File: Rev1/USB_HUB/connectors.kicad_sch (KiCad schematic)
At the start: 24 parts, among them J6 B4B-XH-A, J9 B4B-XH-A, Q1 IRLML2244TRPBF, Q2 IRLML2244TRPBF, Q3 IRLML2244TRPBF, Q4 IRLML2244TRPBF, Q5 IRLML2244TRPBF, Q7 IRLML2244TRPBF

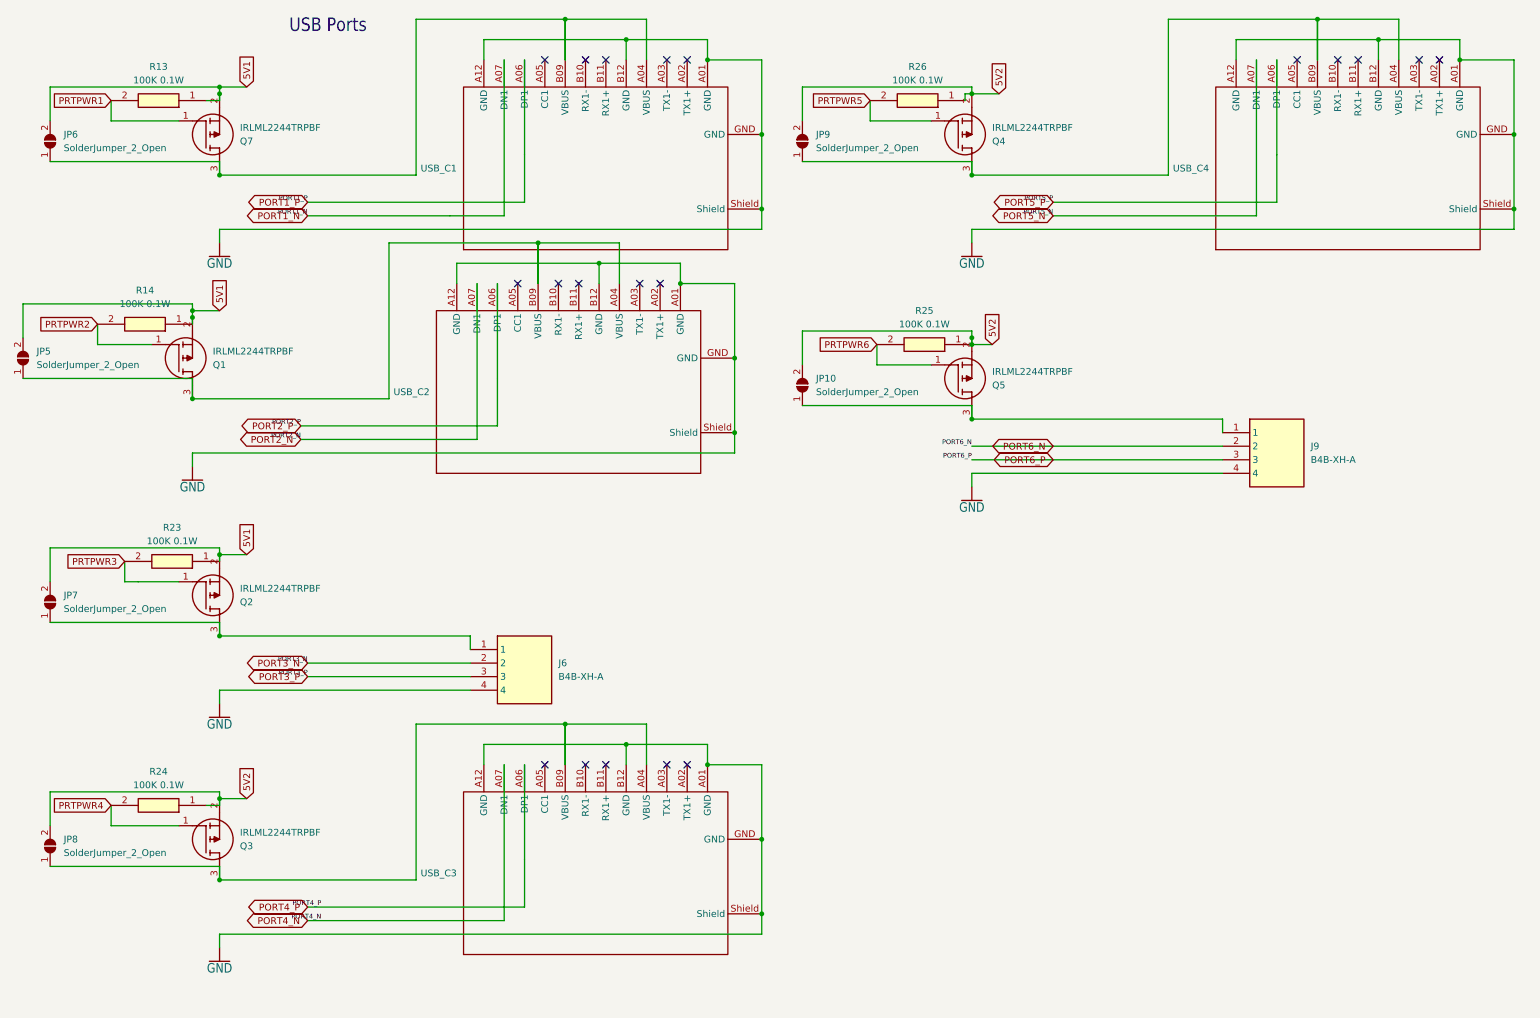
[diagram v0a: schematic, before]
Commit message: USB HUB Updated
Based on TA feedback
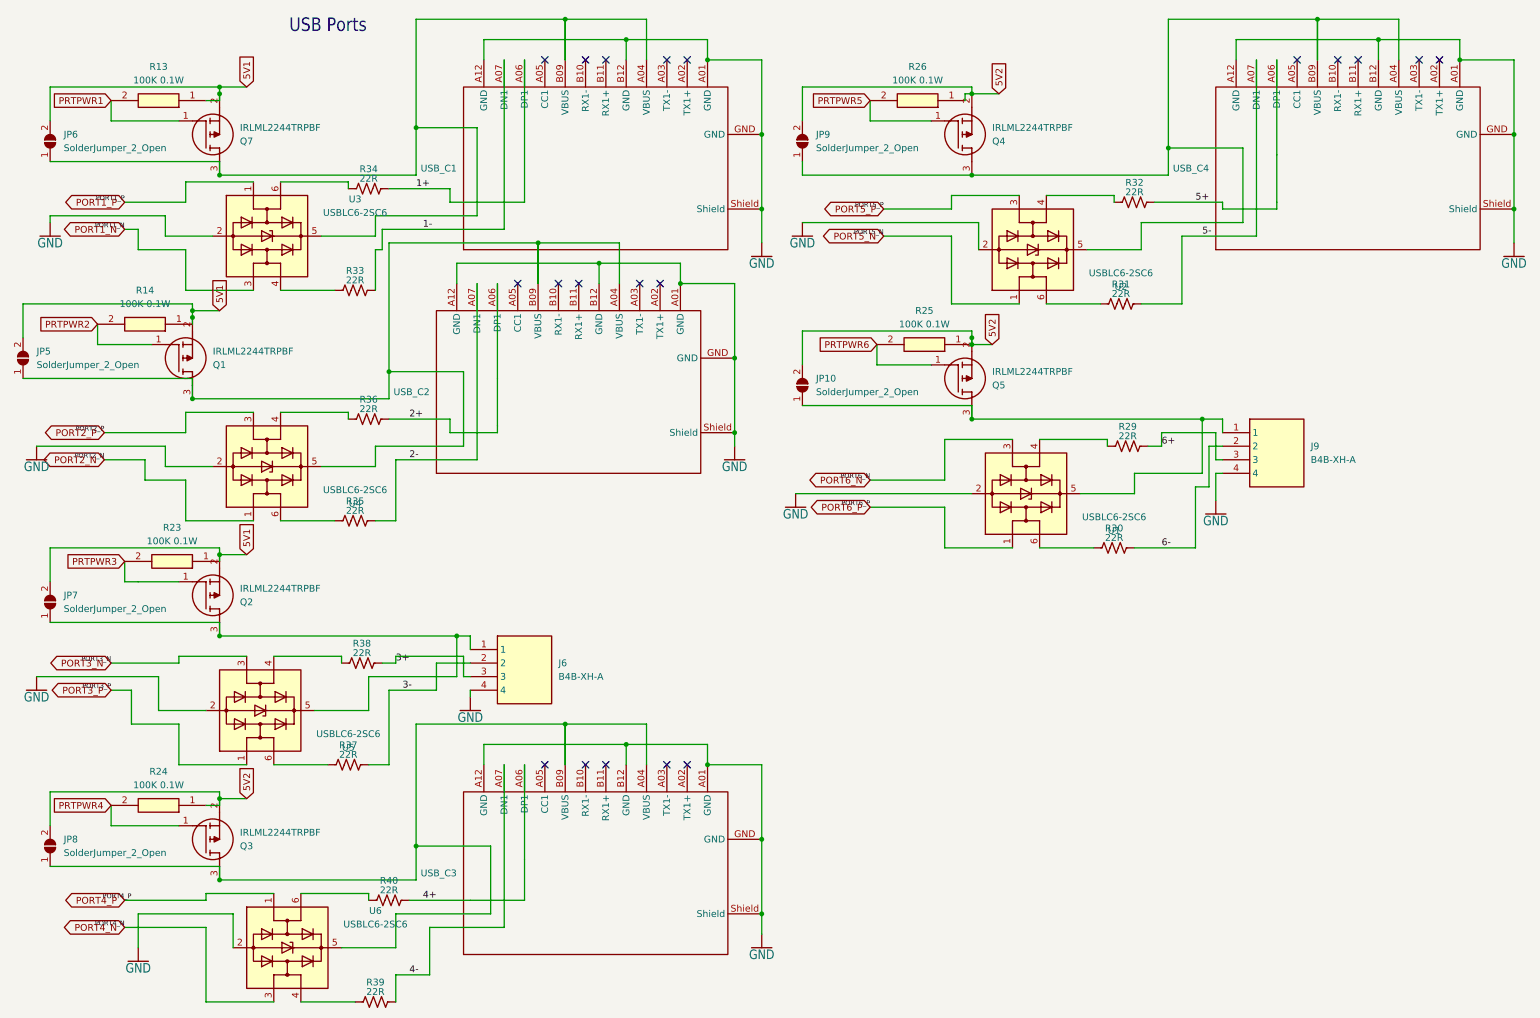
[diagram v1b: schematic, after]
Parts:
- added R29, R30, R31, R32, R33, R34, R35, R36, R37, R38, R39, R40: 22R, Resistor_SMD:R_0603_1608Metric, symbol Device:R_US
- added U1, U2, U3, U4, U5, U6: USBLC6-2SC6, Package_TO_SOT_SMD:SOT-23-6, symbol Power_Protection:USBLC6-2SC6
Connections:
- net GND: now also U1.2 (GND), U2.2 (GND), U3.2 (GND), U4.2 (GND), U5.2 (GND), U6.2 (GND)
- net PORT1_N: now also U3.3 (I/O2); no longer USB_C1.A07 (DN1)
- net PORT1_P: now also U3.1 (I/O1); no longer USB_C1.A06 (DP1)
- net PORT2_N: now also U4.1 (I/O1); no longer USB_C2.A07 (DN1)
- net PORT2_P: now also U4.3 (I/O2); no longer USB_C2.A06 (DP1)
- net PORT3_N: now also U5.3 (I/O2); no longer J6.2
- net PORT3_P: now also U5.1 (I/O1); no longer J6.3
- net PORT4_N: now also U6.3 (I/O2); no longer USB_C3.A07 (DN1)
- net PORT4_P: now also U6.1 (I/O1); no longer USB_C3.A06 (DP1)
- net PORT5_N: now also U2.1 (I/O1); no longer USB_C4.A07 (DN1)
- net PORT5_P: now also U2.3 (I/O2); no longer USB_C4.A06 (DP1)
- net PORT6_N: now also U1.3 (I/O2); no longer J9.2
- net PORT6_P: now also U1.1 (I/O1); no longer J9.3
- net at JP5.1 (A), Q1.3 (D), USB_C2.A04 (VBUS)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: now also U4.5 (VBUS)
- net at JP9.1 (A), Q4.3 (D), USB_C4.A04 (VBUS)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: now also U2.5 (VBUS)
- net at JP8.1 (A), Q3.3 (D), USB_C3.A04 (VBUS)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: now also U6.5 (VBUS)
- net at J6.1, JP7.1 (A), Q2.3 (D): now also U5.5 (VBUS)
- net at JP6.1 (A), Q7.3 (D), USB_C1.A04 (VBUS)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: now also U3.5 (VBUS)
- net at J9.1, JP10.1 (A), Q5.3 (D): now also U1.5 (VBUS)
- new net: R37.2, U5.6 (I/O1)
- new net: R32.2, U2.4 (I/O2)
- new net: R33.2, U3.4 (I/O2)
- new net: R30.2, U1.6 (I/O1)
- new net: R34.2, U3.6 (I/O1)
- new net: R38.2, U5.4 (I/O2)
- new net: R31.2, U2.6 (I/O1)
- new net: R39.2, U6.4 (I/O2)
- new net: R35.2, U4.6 (I/O1)
- new net: R36.2, U4.4 (I/O2)
- new net: R40.2, U6.6 (I/O1)
- new net: R29.2, U1.4 (I/O2)
- new net 1+: R34.1, USB_C1.A06 (DP1)
- new net 1-: R33.1, USB_C1.A07 (DN1)
- new net 2+: R36.1, USB_C2.A06 (DP1)
- new net 2-: R35.1, USB_C2.A07 (DN1)
- new net 3+: J6.3, R38.1
- new net 3-: J6.2, R37.1
- new net 4+: R40.1, USB_C3.A06 (DP1)
- new net 4-: R39.1, USB_C3.A07 (DN1)
- new net 5+: R32.1, USB_C4.A06 (DP1)
- new net 5-: R31.1, USB_C4.A07 (DN1)
- new net 6+: J9.3, R29.1
- new net 6-: J9.2, R30.1
